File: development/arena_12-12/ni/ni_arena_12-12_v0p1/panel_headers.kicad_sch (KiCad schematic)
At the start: 27 parts, among them P1 CONN15, P10 CONN15, P11 CONN15, P12 CONN15, P2 CONN15, P3 CONN15, P4 CONN15, P5 CONN15, P6 CONN15, P7 CONN15, P8 CONN15, P9 CONN15, Q2 MOSFET_NCHAN

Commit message: Worked on schematic adding series termination resistors and buffers.
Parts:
- renumbered C11 to C1, C20 to C10, C21 to C11, C22 to C12, C12 to C2, C13 to C3, C14 to C4, C15 to C5, C16 to C6, C17 to C7, C18 to C8, C19 to C9, Q2 to Q1, R1 to R500, R2 to R501

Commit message: Worked on 12-12 NI arena schematic.
Added schmitt trigger buffers and series termination resistors to
panels headers (not done).
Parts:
- added C35, C36, C37, C38, C39, C40, C41, C42, C43, C44, C45, C46, C47, C48, C49, C50, C51, C52, C53, C54, C55, C56, C57, C58, C59, C60, C61, C62, C63, C64, C65, C66, C67, C68, C69, C70, C71, C72, C73, C74, C75, C76, C77, C78, C79, C80, C81, C82: 0.1uF, symbol Device:C_Small
- added R175, R176, R177, R178, R179, R180, R181, R182, R183, R184, R185, R186, R187, R188, R189, R190, R191, R192, R193, R194, R195, R196, R197, R198, R199, R200, R201, R202, R203, R204, R205, R206, R207, R208, R209, R210, R211, R212, R213, R214, R215, R216, R217, R218, R219, R220, R221, R222, R223, R224, R225, R226, R227, R228, R229, R230, R231, R232, R233, R234, R235, R236, R237, R238, R239, R240, R241, R242, R243, R244, R245, R246, R247, R248, R249, R250, R251, R252, R253, R254, R255, R256, R257, R258, R29, R30, R31, R32, R33, R34, R35, R36, R37, R38, R39, R40: 33, symbol Device:R
- added U39, U40, U41, U42, U43, U44, U45, U46, U47, U48, U49, U50, U51, U52, U53, U54, U55, U56, U57, U58, U59, U60, U61, U62, U63, U64, U65, U66, U67, U68, U69, U70, U71, U72, U73, U74, U75, U76, U77, U78, U79, U80, U81, U82, U83, U84, U85, U86: 74LVC2G17, symbol 74xGxx:74LVC2G17
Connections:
- net GND: now also C35.2, C36.2, C37.2, C38.2, C39.2, C40.2, C41.2, C42.2, C43.2, C44.2, C45.2, C46.2, C47.2, C48.2, C49.2, C50.2, C51.2, C52.2, C53.2, C54.2, C55.2, C56.2, C57.2, C58.2, C59.2, C60.2, C61.2, C62.2, C63.2, C64.2, C65.2, C66.2, C67.2, C68.2, C69.2, C70.2, C71.2, C72.2, C73.2, C74.2, C75.2, C76.2, C77.2, C78.2, C79.2, C80.2, C81.2, C82.2, U39.2 (GND), U40.2 (GND), U41.2 (GND), U42.2 (GND), U43.2 (GND), U44.2 (GND), U45.2 (GND), U46.2 (GND), U47.2 (GND), U48.2 (GND), U49.2 (GND), U50.2 (GND), U51.2 (GND), U52.2 (GND), U53.2 (GND), U54.2 (GND), U55.2 (GND), U56.2 (GND), U57.2 (GND), U58.2 (GND), U59.2 (GND), U60.2 (GND), U61.2 (GND), U62.2 (GND), U63.2 (GND), U64.2 (GND), U65.2 (GND), U66.2 (GND), U67.2 (GND), U68.2 (GND), U69.2 (GND), U70.2 (GND), U71.2 (GND), U72.2 (GND), U73.2 (GND), U74.2 (GND), U75.2 (GND), U76.2 (GND), U77.2 (GND), U78.2 (GND), U79.2 (GND), U80.2 (GND), U81.2 (GND), U82.2 (GND), U83.2 (GND), U84.2 (GND), U85.2 (GND), U86.2 (GND)
- net PAN5V.CS_00: no longer P1.7, P2.7, P3.7, P4.7, P5.7, P6.7, P7.7, P8.7
- net PAN5V.CS_01: no longer P1.8, P2.8, P3.8, P4.8, P5.8, P6.8, P7.8, P8.8
- net PAN5V.CS_02: no longer P1.9, P2.9, P3.9, P4.9, P5.9, P6.9, P7.9, P8.9
- net PAN5V.CS_03: no longer P1.10, P2.10, P3.10, P4.10, P5.10, P6.10, P7.10, P8.10
- net PAN5V.CS_04: no longer P1.11, P2.11, P3.11, P4.11, P5.11, P6.11, P7.11, P8.11
- net PAN5V.CS_05: no longer P1.12, P2.12, P3.12, P4.12, P5.12, P6.12, P7.12, P8.12
- net PAN5V.CS_06: no longer P1.13, P2.13, P3.13, P4.13, P5.13, P6.13, P7.13, P8.13
- net PAN5V.CS_07: no longer P1.14, P2.14, P3.14, P4.14, P5.14, P6.14, P7.14, P8.14
- net PAN5V.EXT_INT: now also U44.1, U50.1, U56.1, U62.1, U68.1, U74.1, U80.1, U86.1; no longer P1.15, P2.15, P3.15, P4.15, P5.15, P6.15, P7.15, P8.15
- net PAN5V.MISO_00: now also R31.1; no longer P1.6
- net PAN5V.MISO_01: now also R177.1; no longer P2.6
- net PAN5V.MISO_02: now also R189.1; no longer P3.6
- net PAN5V.MISO_03: now also R201.1; no longer P4.6
- net PAN5V.MISO_04: now also R213.1; no longer P5.6
- net PAN5V.MISO_05: now also R225.1; no longer P6.6
- net PAN5V.MISO_06: now also R237.1; no longer P7.6
- net PAN5V.MISO_07: now also R249.1; no longer P8.6
- net PAN5V.MOSI_00: now also U39.3; no longer P1.5
- net PAN5V.MOSI_01: now also U45.3; no longer P2.5
- net PAN5V.MOSI_02: now also U51.3; no longer P3.5
- net PAN5V.MOSI_03: now also U57.3; no longer P4.5
- net PAN5V.MOSI_04: now also U63.3; no longer P5.5
- net PAN5V.MOSI_05: now also U69.3; no longer P6.5
- net PAN5V.MOSI_06: now also U75.3; no longer P7.5
- net PAN5V.MOSI_07: now also U81.3; no longer P8.5
- net PAN5V.SCK_02: no longer P3.4
- net PAN5V.SCK_03: no longer P4.4
- net PAN5V.SCK_04: no longer P5.4
- net PAN5V.SCK_05: no longer P6.4
- net RESET: no longer P10.3, P11.3, P12.3, P9.3
- net PAN5V.SCK_00 renamed SCK_0_H1_P01
- net SCK_0_H1_P01: now also R29.2; no longer P7.4
- net PAN5V.SCK_01 renamed SCK_1_H1_P02
- net SCK_1_H1_P02: now also R175.2; no longer P8.4
- new net: R229.1, U71.4
- new net: R194.1, U54.6
- new net: R247.1, U81.6
- new net: R245.1, U79.4
- new net: R238.1, U76.6
- new net: R256.1, U85.6
- new net: R196.1, U55.6
- new net: R208.1, U61.6
- new net: R176.1, U45.4
- new net: R206.1, U60.6
- new net: R184.1, U49.6
- new net: R193.1, U53.4
- new net: R257.1, U85.4
- new net: R35.1, U41.4
- new net: R199.1, U57.6
- new net: R30.1, U39.4
- new net: R217.1, U65.4
- new net: R187.1, U51.6
- new net: R212.1, U63.4
- new net: R255.1, U84.4
- new net: R210.1, U62.6
- new net: R205.1, U59.4
- new net: R250.1, U82.6
- new net: R211.1, U63.6
- new net: R178.1, U46.6
- new net: R246.1, U80.6
- new net: R226.1, U70.6
- new net: R188.1, U51.4
- new net: R248.1, U81.4
- new net: R215.1, U64.4
- new net: R231.1, U72.4
- new net: R243.1, U78.4
- new net: R239.1, U76.4
- new net: R233.1, U73.4
- new net: R181.1, U47.4
- new net: R236.1, U75.4
- new net: R195.1, U54.4
- new net: R230.1, U72.6
- new net: R185.1, U49.4
- new net: R183.1, U48.4
- new net: R244.1, U79.6
- new net: R227.1, U70.4
- new net: R197.1, U55.4
- new net: R214.1, U64.6
- new net: R38.1, U43.6
- new net: R39.1, U43.4
- new net: R203.1, U58.4
- new net: R254.1, U84.6
- new net: R190.1, U52.6
- new net: R218.1, U66.6
- new net: R175.1, U45.6
- new net: R216.1, U65.6
- new net: R180.1, U47.6
- new net: R224.1, U69.4
- new net: R223.1, U69.6
- new net: R251.1, U82.4
- new net: R204.1, U59.6
- new net: R192.1, U53.6
- new net: R228.1, U71.6
- new net: R202.1, U58.6
- new net: R191.1, U52.4
- new net: R36.1, U42.6
- new net: R209.1, U61.4
- new net: R258.1, U86.6
- new net: R179.1, U46.4
- new net: R207.1, U60.4
- new net: R200.1, U57.4
- new net: R234.1, U74.6
- new net: R220.1, U67.6
- new net: R198.1, U56.6
- new net: R221.1, U67.4
- new net: R182.1, U48.6
- new net: R33.1, U40.4
- new net: R242.1, U78.6
- new net: R29.1, U39.6
- new net: R252.1, U83.6
- new net: R240.1, U77.6
- new net: R241.1, U77.4
- new net: R37.1, U42.4
- new net: R219.1, U66.4
- new net: R34.1, U41.6
- new net: R235.1, U75.6
- new net: R40.1, U44.6
- new net: R232.1, U73.6
- new net: R253.1, U83.4
- new net: R32.1, U40.6
- new net: R186.1, U50.6
- new net: R222.1, U68.6
- new net +3.3V: C35.1, C36.1, C37.1, C38.1, C39.1, C40.1, C41.1, C42.1, C43.1, C44.1, C45.1, C46.1, C47.1, C48.1, C49.1, C50.1, C51.1, C52.1, C53.1, C54.1, C55.1, C56.1, C57.1, C58.1, C59.1, C60.1, C61.1, C62.1, C63.1, C64.1, C65.1, C66.1, C67.1, C68.1, C69.1, C70.1, C71.1, C72.1, C73.1, C74.1, C75.1, C76.1, C77.1, C78.1, C79.1, C80.1, C81.1, C82.1, U39.5 (VCC), U40.5 (VCC), U41.5 (VCC), U42.5 (VCC), U43.5 (VCC), U44.5 (VCC), U45.5 (VCC), U46.5 (VCC), U47.5 (VCC), U48.5 (VCC), U49.5 (VCC), U50.5 (VCC), U51.5 (VCC), U52.5 (VCC), U53.5 (VCC), U54.5 (VCC), U55.5 (VCC), U56.5 (VCC), U57.5 (VCC), U58.5 (VCC), U59.5 (VCC), U60.5 (VCC), U61.5 (VCC), U62.5 (VCC), U63.5 (VCC), U64.5 (VCC), U65.5 (VCC), U66.5 (VCC), U67.5 (VCC), U68.5 (VCC), U69.5 (VCC), U70.5 (VCC), U71.5 (VCC), U72.5 (VCC), U73.5 (VCC), U74.5 (VCC), U75.5 (VCC), U76.5 (VCC), U77.5 (VCC), U78.5 (VCC), U79.5 (VCC), U80.5 (VCC), U81.5 (VCC), U82.5 (VCC), U83.5 (VCC), U84.5 (VCC), U85.5 (VCC), U86.5 (VCC)
- new net CS_00_P01: P1.7, R32.2
- new net CS_00_P02: P2.7, R178.2
- new net CS_00_P03: P3.7, R190.2
- new net CS_00_P04: P4.7, R202.2
- new net CS_00_P05: P5.7, R214.2
- new net CS_00_P06: P6.7, R226.2
- new net CS_00_P07: P7.7, R238.2
- new net CS_00_P08: P8.7, R250.2
- new net CS_01_P01: P1.8, R33.2
- new net CS_01_P02: P2.8, R179.2
- new net CS_01_P03: P3.8, R191.2
- new net CS_01_P04: P4.8, R203.2
- new net CS_01_P05: P5.8, R215.2
- new net CS_01_P06: P6.8, R227.2
- new net CS_01_P07: P7.8, R239.2
- new net CS_01_P08: P8.8, R251.2
- new net CS_02_P01: P1.9, R34.2
- new net CS_02_P02: P2.9, R180.2
- new net CS_02_P03: P3.9, R192.2
- new net CS_02_P04: P4.9, R204.2
- new net CS_02_P05: P5.9, R216.2
- new net CS_02_P06: P6.9, R228.2
- new net CS_02_P07: P7.9, R240.2
- new net CS_02_P08: P8.9, R252.2
- new net CS_03_P01: P1.10, R35.2
- new net CS_03_P02: P2.10, R181.2
- new net CS_03_P03: P3.10, R193.2
- new net CS_03_P04: P4.10, R205.2
- new net CS_03_P05: P5.10, R217.2
- new net CS_03_P06: P6.10, R229.2
- new net CS_03_P07: P7.10, R241.2
- new net CS_03_P08: P8.10, R253.2
- new net CS_04_P01: P1.11, R36.2
- new net CS_04_P02: P2.11, R182.2
- new net CS_04_P03: P3.11, R194.2
- new net CS_04_P04: P4.11, R206.2
- new net CS_04_P05: P5.11, R218.2
- new net CS_04_P06: P6.11, R230.2
- new net CS_04_P07: P7.11, R242.2
- new net CS_04_P08: P8.11, R254.2
- new net CS_05_P01: P1.12, R37.2
- new net CS_05_P02: P2.12, R183.2
- new net CS_05_P03: P3.12, R195.2
- new net CS_05_P04: P4.12, R207.2
- new net CS_05_P05: P5.12, R219.2
- new net CS_05_P06: P6.12, R231.2
- new net CS_05_P07: P7.12, R243.2
- new net CS_05_P08: P8.12, R255.2
- new net CS_06_P01: P1.13, R38.2
- new net CS_06_P02: P2.13, R184.2
- new net CS_06_P03: P3.13, R196.2
- new net CS_06_P04: P4.13, R208.2
- new net CS_06_P05: P5.13, R220.2
- new net CS_06_P06: P6.13, R232.2
- new net CS_06_P07: P7.13, R244.2
- new net CS_06_P08: P8.13, R256.2
- new net CS_07_P01: P1.14, R39.2
- new net CS_07_P02: P2.14, R185.2
- new net CS_07_P03: P3.14, R197.2
- new net CS_07_P04: P4.14, R209.2
- new net CS_07_P05: P5.14, R221.2
- new net CS_07_P06: P6.14, R233.2
- new net CS_07_P07: P7.14, R245.2
- new net CS_07_P08: P8.14, R257.2
- new net EXT_INT_P01: P1.15, R40.2
- new net EXT_INT_P02: P2.15, R186.2
- new net EXT_INT_P03: P3.15, R198.2
- new net EXT_INT_P04: P4.15, R210.2
- new net EXT_INT_P05: P5.15, R222.2
- new net EXT_INT_P06: P6.15, R234.2
- new net EXT_INT_P07: P7.15, R246.2
- new net EXT_INT_P08: P8.15, R258.2
- new net MISO_00_P01: P1.6, R31.2
- new net MISO_01_P02: P2.6, R177.2
- new net MISO_02_P03: P3.6, R189.2
- new net MISO_03_P04: P4.6, R201.2
- new net MISO_04_P05: P5.6, R213.2
- new net MISO_05_P06: P6.6, R225.2
- new net MISO_06_P07: P7.6, R237.2
- new net MISO_07_P08: P8.6, R249.2
- new net MOSI_00_P01: P1.5, R30.2
- new net MOSI_01_P02: P2.5, R176.2
- new net MOSI_02_P03: P3.5, R188.2
- new net MOSI_03_P04: P4.5, R200.2
- new net MOSI_04_P05: P5.5, R212.2
- new net MOSI_05_P06: P6.5, R224.2
- new net MOSI_06_P07: P7.5, R236.2
- new net MOSI_07_P08: P8.5, R248.2
- new net PAN5V.CS_0_P01: U40.1
- new net PAN5V.CS_0_P02: U46.1
- new net PAN5V.CS_0_P03: U52.1
- new net PAN5V.CS_0_P04: U58.1
- new net PAN5V.CS_0_P05: U64.1
- new net PAN5V.CS_0_P06: U70.1
- new net PAN5V.CS_0_P07: U76.1
- new net PAN5V.CS_0_P08: U82.1
- new net PAN5V.CS_1_P01: U40.3
- new net PAN5V.CS_1_P02: U46.3
- new net PAN5V.CS_1_P03: U52.3
- new net PAN5V.CS_1_P04: U58.3
- new net PAN5V.CS_1_P05: U64.3
- new net PAN5V.CS_1_P06: U70.3
- new net PAN5V.CS_1_P07: U76.3
- new net PAN5V.CS_1_P08: U82.3
- new net PAN5V.CS_2_P01: U41.1
- new net PAN5V.CS_2_P02: U47.1
- new net PAN5V.CS_2_P03: U53.1
- new net PAN5V.CS_2_P04: U59.1
- new net PAN5V.CS_2_P05: U65.1
- new net PAN5V.CS_2_P06: U71.1
- new net PAN5V.CS_2_P07: U77.1
- new net PAN5V.CS_2_P08: U83.1
- new net PAN5V.CS_3_P01: U41.3
- new net PAN5V.CS_3_P02: U47.3
- new net PAN5V.CS_3_P03: U53.3
- new net PAN5V.CS_3_P04: U59.3
- new net PAN5V.CS_3_P05: U65.3
- new net PAN5V.CS_3_P06: U71.3
- new net PAN5V.CS_3_P07: U77.3
- new net PAN5V.CS_3_P08: U83.3
- new net PAN5V.CS_4_P01: U42.1
- new net PAN5V.CS_4_P02: U48.1
- new net PAN5V.CS_4_P03: U54.1
- new net PAN5V.CS_4_P04: U60.1
- new net PAN5V.CS_4_P05: U66.1
- new net PAN5V.CS_4_P06: U72.1
- new net PAN5V.CS_4_P07: U78.1
- new net PAN5V.CS_4_P08: U84.1
- new net PAN5V.CS_5_P01: U42.3
- new net PAN5V.CS_5_P02: U48.3
- new net PAN5V.CS_5_P03: U54.3
- new net PAN5V.CS_5_P04: U60.3
- new net PAN5V.CS_5_P05: U66.3
- new net PAN5V.CS_5_P06: U72.3
- new net PAN5V.CS_5_P07: U78.3
- new net PAN5V.CS_5_P08: U84.3
- new net PAN5V.CS_6_P01: U43.1
- new net PAN5V.CS_6_P02: U49.1
- new net PAN5V.CS_6_P03: U55.1
- new net PAN5V.CS_6_P04: U61.1
- new net PAN5V.CS_6_P05: U67.1
- new net PAN5V.CS_6_P06: U73.1
- new net PAN5V.CS_6_P07: U79.1
- new net PAN5V.CS_6_P08: U85.1
- new net PAN5V.CS_7_P01: U43.3
- new net PAN5V.CS_7_P02: U49.3
- new net PAN5V.CS_7_P03: U55.3
- new net PAN5V.CS_7_P04: U61.3
- new net PAN5V.CS_7_P05: U67.3
- new net PAN5V.CS_7_P06: U73.3
- new net PAN5V.CS_7_P07: U79.3
- new net PAN5V.CS_7_P08: U85.3
- new net PAN5V.SCK_0_H1: U39.1
- new net PAN5V.SCK_0_H2: U75.1
- new net PAN5V.SCK_1_H1: U45.1
- new net PAN5V.SCK_1_H2: U81.1
- new net PAN5V.SCK_2_H1: U51.1
- new net PAN5V.SCK_3_H1: U57.1
- new net PAN5V.SCK_4_H1: U63.1
- new net PAN5V.SCK_5_H1: U69.1
- new net SCK_0_H2_P07: P7.4, R235.2
- new net SCK_1_H2_P08: P8.4, R247.2
- new net SCK_2_H1_P03: P3.4, R187.2
- new net SCK_3_H1_P04: P4.4, R199.2
- new net SCK_4_H1_P05: P5.4, R211.2
- new net SCK_5_H1_P06: P6.4, R223.2
- no-connect marks 0 -> 16
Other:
- note added: "SI2302-TP Digikey SI2302-TPMSCT-ND LCSC C4748714 or ME2306D LCSC C165220"
- note removed: "SI2302-TP Digikey SI2302-TPMSCT-ND LCSC C4748714"
- moved on the sheet: C1, C10, C11, C12, C9, P1, P10, P11, P12, P9, Q1, R500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

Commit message: More work on 12-12 NI arena panels headers sheet.
Changes schmitt trigger power to 5V instead 3.3V.  Finished Panels
column P9.
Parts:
- added C84, C85, C86, C87, C88, C89: 0.1uF, symbol Device:C_Small
- added R259, R260, R261, R262, R263, R264, R265, R266, R267, R268, R269, R270: 33, symbol Device:R
- added U87, U88, U89, U90, U91, U92: 74LVC2G17, symbol 74xGxx:74LVC2G17
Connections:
- net +3.3V is gone; now on net +5V: C35.1, C36.1, C37.1, C38.1, C39.1, C40.1, C41.1, C42.1, C43.1, C44.1, C45.1, C46.1, C47.1, C48.1, C49.1, C50.1, C51.1, C52.1, C53.1, C54.1, C55.1, C56.1, C57.1, C58.1, C59.1, C60.1, C61.1, C62.1, C63.1, C64.1, C65.1, C66.1, C67.1, C68.1, C69.1, C70.1, C71.1, C72.1, C73.1, C74.1, C75.1, C76.1, C77.1, C78.1, C79.1, C80.1, C81.1, C82.1, U39.5 (VCC), U40.5 (VCC), U41.5 (VCC), U42.5 (VCC), U43.5 (VCC), U44.5 (VCC), U45.5 (VCC), U46.5 (VCC), U47.5 (VCC), U48.5 (VCC), U49.5 (VCC), U50.5 (VCC), U51.5 (VCC), U52.5 (VCC), U53.5 (VCC), U54.5 (VCC), U55.5 (VCC), U56.5 (VCC), U57.5 (VCC), U58.5 (VCC), U59.5 (VCC), U60.5 (VCC), U61.5 (VCC), U62.5 (VCC), U63.5 (VCC), U64.5 (VCC), U65.5 (VCC), U66.5 (VCC), U67.5 (VCC), U68.5 (VCC), U69.5 (VCC), U70.5 (VCC), U71.5 (VCC), U72.5 (VCC), U73.5 (VCC), U74.5 (VCC), U75.5 (VCC), U76.5 (VCC), U77.5 (VCC), U78.5 (VCC), U79.5 (VCC), U80.5 (VCC), U81.5 (VCC), U82.5 (VCC), U83.5 (VCC), U84.5 (VCC), U85.5 (VCC), U86.5 (VCC)
- net +5V: now also C84.1, C85.1, C86.1, C87.1, C88.1, C89.1, U87.5 (VCC), U88.5 (VCC), U89.5 (VCC), U90.5 (VCC), U91.5 (VCC), U92.5 (VCC)
- net GND: now also C84.2, C85.2, C86.2, C87.2, C88.2, C89.2, U87.2 (GND), U88.2 (GND), U89.2 (GND), U90.2 (GND), U91.2 (GND), U92.2 (GND)
- net PAN5V.CS_00: no longer P9.7
- net PAN5V.CS_01: no longer P9.8
- net PAN5V.CS_02: no longer P9.9
- net PAN5V.CS_03: no longer P9.10
- net PAN5V.CS_04: no longer P9.11
- net PAN5V.CS_05: no longer P9.12
- net PAN5V.CS_06: no longer P9.13
- net PAN5V.CS_07: no longer P9.14
- net PAN5V.CS_0_P09: now also U88.1
- net PAN5V.CS_1_P09: now also U88.3
- net PAN5V.CS_2_P09: now also U89.1
- net PAN5V.CS_3_P09: now also U89.3
- net PAN5V.CS_4_P09: now also U90.1
- net PAN5V.CS_5_P09: now also U90.3
- net PAN5V.CS_6_P09: now also U91.1
- net PAN5V.CS_7_P09: now also U91.3
- net PAN5V.EXT_INT: now also U92.1; no longer P9.15
- net PAN5V.MISO_08: now also R261.1; no longer P9.6
- net PAN5V.MOSI_08: now also U87.3; no longer P9.5
- net PAN5V.SCK_2_H2: now also U87.1
- net RESET: now also P9.3
- net PAN5V.SCK_02 renamed SCK_2_H2_P09
- net SCK_2_H2_P09: now also R259.2
- new net: R268.1, U91.6
- new net: R265.1, U89.4
- new net: R266.1, U90.6
- new net: R264.1, U89.6
- new net: R263.1, U88.4
- new net: R269.1, U91.4
- new net: R262.1, U88.6
- new net: R270.1, U92.6
- new net: R260.1, U87.4
- new net: R267.1, U90.4
- new net: R259.1, U87.6
- new net CS_00_P09: P9.7, R262.2
- new net CS_01_P09: P9.8, R263.2
- new net CS_02_P09: P9.9, R264.2
- new net CS_03_P09: P9.10, R265.2
- new net CS_04_P09: P9.11, R266.2
- new net CS_05_P09: P9.12, R267.2
- new net CS_06_P09: P9.13, R268.2
- new net CS_07_P09: P9.14, R269.2
- new net EXT_INT_P09: P9.15, R270.2
- new net MISO_08_P09: P9.6, R261.2
- new net MOSI_08_P09: P9.5, R260.2
- no-connect marks 16 -> 18

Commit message: Finished initial schematic for 12-12 NI with schmitt buffers.
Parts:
- added C100, C101, C102, C103, C104, C105, C106, C107, C90, C91, C92, C93, C94, C95, C96, C97, C98, C99: 0.1uF, symbol Device:C_Small
- added R271, R272, R273, R274, R275, R276, R277, R278, R279, R280, R281, R282, R283, R284, R285, R286, R287, R288, R289, R290, R291, R292, R293, R294, R295, R296, R297, R298, R299, R300, R301, R302, R303, R304, R305, R306: 33, symbol Device:R
- added U100, U101, U102, U103, U104, U105, U106, U107, U108, U109, U110, U93, U94, U95, U96, U97, U98, U99: 74LVC2G17, symbol 74xGxx:74LVC2G17
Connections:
- net +5V: now also C100.1, C101.1, C102.1, C103.1, C104.1, C105.1, C106.1, C107.1, C90.1, C91.1, C92.1, C93.1, C94.1, C95.1, C96.1, C97.1, C98.1, C99.1, U100.5 (VCC), U101.5 (VCC), U102.5 (VCC), U103.5 (VCC), U104.5 (VCC), U105.5 (VCC), U106.5 (VCC), U107.5 (VCC), U108.5 (VCC), U109.5 (VCC), U110.5 (VCC), U93.5 (VCC), U94.5 (VCC), U95.5 (VCC), U96.5 (VCC), U97.5 (VCC), U98.5 (VCC), U99.5 (VCC)
- net GND: now also C100.2, C101.2, C102.2, C103.2, C104.2, C105.2, C106.2, C107.2, C90.2, C91.2, C92.2, C93.2, C94.2, C95.2, C96.2, C97.2, C98.2, C99.2, U100.2 (GND), U101.2 (GND), U102.2 (GND), U103.2 (GND), U104.2 (GND), U105.2 (GND), U106.2 (GND), U107.2 (GND), U108.2 (GND), U109.2 (GND), U110.2 (GND), U93.2 (GND), U94.2 (GND), U95.2 (GND), U96.2 (GND), U97.2 (GND), U98.2 (GND), U99.2 (GND)
- net PAN5V.CS_0_P10: now also U94.1
- net PAN5V.CS_0_P11: now also U100.1
- net PAN5V.CS_0_P12: now also U106.1
- net PAN5V.CS_1_P10: now also U94.3
- net PAN5V.CS_1_P11: now also U100.3
- net PAN5V.CS_1_P12: now also U106.3
- net PAN5V.CS_2_P10: now also U95.1
- net PAN5V.CS_2_P11: now also U101.1
- net PAN5V.CS_2_P12: now also U107.1
- net PAN5V.CS_3_P10: now also U95.3
- net PAN5V.CS_3_P11: now also U101.3
- net PAN5V.CS_3_P12: now also U107.3
- net PAN5V.CS_4_P10: now also U96.1
- net PAN5V.CS_4_P11: now also U102.1
- net PAN5V.CS_4_P12: now also U108.1
- net PAN5V.CS_5_P10: now also U96.3
- net PAN5V.CS_5_P11: now also U102.3
- net PAN5V.CS_5_P12: now also U108.3
- net PAN5V.CS_6_P10: now also U97.1
- net PAN5V.CS_6_P11: now also U103.1
- net PAN5V.CS_6_P12: now also U109.1
- net PAN5V.CS_7_P10: now also U97.3
- net PAN5V.CS_7_P11: now also U103.3
- net PAN5V.CS_7_P12: now also U109.3
- net PAN5V.EXT_INT: now also U104.1, U110.1, U98.1; no longer P10.15, P11.15, P12.15
- net PAN5V.MISO_09: now also R273.1; no longer P10.6
- net PAN5V.MISO_10: now also R285.1; no longer P11.6
- net PAN5V.MISO_11: now also R297.1; no longer P12.6
- net PAN5V.MOSI_09: now also U93.3; no longer P10.5
- net PAN5V.MOSI_10: now also U99.3; no longer P11.5
- net PAN5V.MOSI_11: now also U105.3; no longer P12.5
- net PAN5V.SCK_3_H2: now also U93.1
- net PAN5V.SCK_4_H2: now also U99.1
- net PAN5V.SCK_5_H2: now also U105.1
- net RESET: now also P10.3, P11.3, P12.3
- removed net PAN5V.CS_00: P10.7, P11.7, P12.7
- removed net PAN5V.CS_01: P10.8, P11.8, P12.8
- removed net PAN5V.CS_02: P10.9, P11.9, P12.9
- removed net PAN5V.CS_03: P10.10, P11.10, P12.10
- removed net PAN5V.CS_04: P10.11, P11.11, P12.11
- removed net PAN5V.CS_05: P10.12, P11.12, P12.12
- removed net PAN5V.CS_06: P10.13, P11.13, P12.13
- removed net PAN5V.CS_07: P10.14, P11.14, P12.14
- net PAN5V.SCK_03 renamed SCK_3_H2_P10
- net SCK_3_H2_P10: now also R271.2
- net PAN5V.SCK_04 renamed SCK_4_H2_P11
- net SCK_4_H2_P11: now also R283.2
- net PAN5V.SCK_05 renamed SCK_5_H2_P12
- net SCK_5_H2_P12: now also R295.2
- new net: R287.1, U100.4
- new net: R304.1, U109.6
- new net: R279.1, U96.4
- new net: R294.1, U104.6
- new net: R281.1, U97.4
- new net: R301.1, U107.4
- new net: R272.1, U93.4
- new net: R293.1, U103.4
- new net: R306.1, U110.6
- new net: R280.1, U97.6
- new net: R303.1, U108.4
- new net: R300.1, U107.6
- new net: R289.1, U101.4
- new net: R277.1, U95.4
- new net: R286.1, U100.6
- new net: R283.1, U99.6
- new net: R278.1, U96.6
- new net: R298.1, U106.6
- new net: R276.1, U95.6
- new net: R291.1, U102.4
- new net: R282.1, U98.6
- new net: R271.1, U93.6
- new net: R288.1, U101.6
- new net: R302.1, U108.6
- new net: R295.1, U105.6
- new net: R292.1, U103.6
- new net: R290.1, U102.6
- new net: R284.1, U99.4
- new net: R275.1, U94.4
- new net: R299.1, U106.4
- new net: R296.1, U105.4
- new net: R305.1, U109.4
- new net: R274.1, U94.6
- new net CS_00_P10: P10.7, R274.2
- new net CS_00_P11: P11.7, R286.2
- new net CS_00_P12: P12.7, R298.2
- new net CS_01_P10: P10.8, R275.2
- new net CS_01_P11: P11.8, R287.2
- new net CS_01_P12: P12.8, R299.2
- new net CS_02_P10: P10.9, R276.2
- new net CS_02_P11: P11.9, R288.2
- new net CS_02_P12: P12.9, R300.2
- new net CS_03_P10: P10.10, R277.2
- new net CS_03_P11: P11.10, R289.2
- new net CS_03_P12: P12.10, R301.2
- new net CS_04_P10: P10.11, R278.2
- new net CS_04_P11: P11.11, R290.2
- new net CS_04_P12: P12.11, R302.2
- new net CS_05_P10: P10.12, R279.2
- new net CS_05_P11: P11.12, R291.2
- new net CS_05_P12: P12.12, R303.2
- new net CS_06_P10: P10.13, R280.2
- new net CS_06_P11: P11.13, R292.2
- new net CS_06_P12: P12.13, R304.2
- new net CS_07_P10: P10.14, R281.2
- new net CS_07_P11: P11.14, R293.2
- new net CS_07_P12: P12.14, R305.2
- new net EXT_INT_P10: P10.15, R282.2
- new net EXT_INT_P11: P11.15, R294.2
- new net EXT_INT_P12: P12.15, R306.2
- new net MISO_09_P10: P10.6, R273.2
- new net MISO_10_P11: P11.6, R285.2
- new net MISO_11_P12: P12.6, R297.2
- new net MOSI_09_P10: P10.5, R272.2
- new net MOSI_10_P11: P11.5, R284.2
- new net MOSI_11_P12: P12.5, R296.2
- no-connect marks 18 -> 24
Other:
- moved on the sheet: C1, C2, C3, C35, C36, C37, C38, C39, C4, C40, C41, C42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

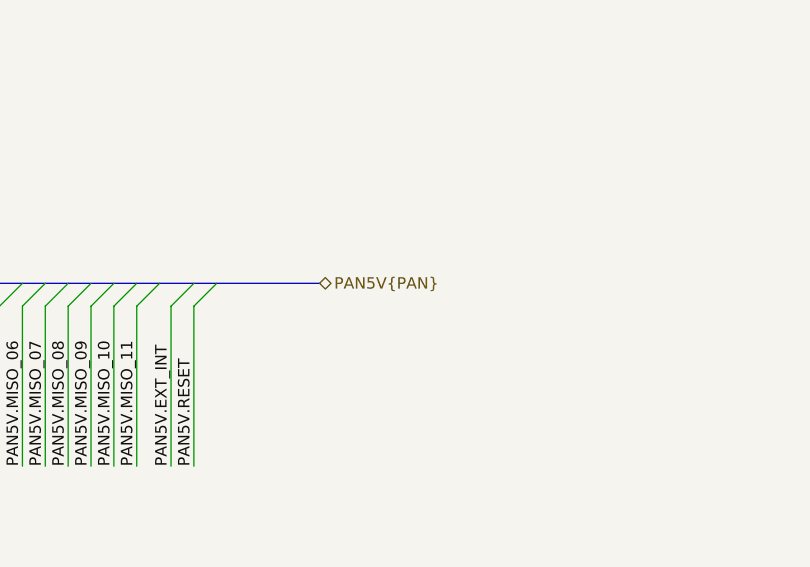
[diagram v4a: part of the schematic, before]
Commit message: Worked on NI 12-12 arena schematic.
Set up new bus definitions and started working through DRC issues.
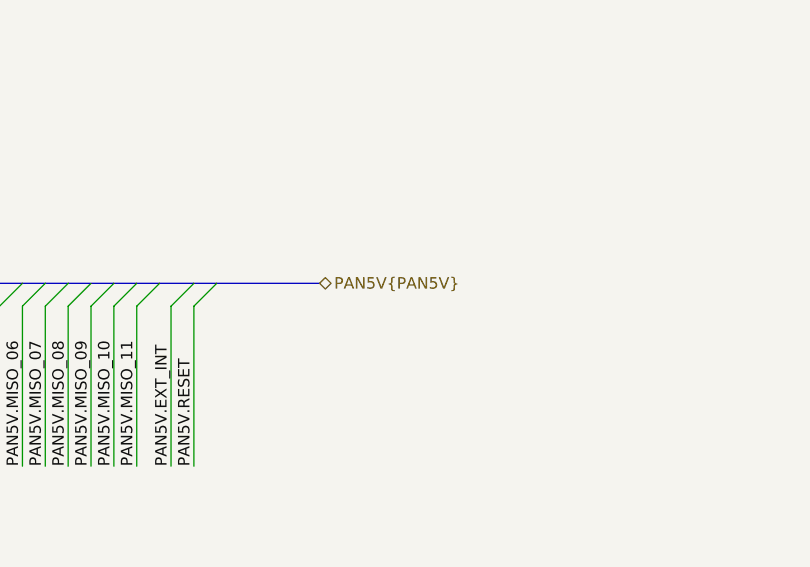
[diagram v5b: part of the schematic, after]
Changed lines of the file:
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@@
 		)
 	)
-	(hierarchical_label "PAN5V{PAN}"
+	(hierarchical_label "PAN5V{PAN5V}"
 		(shape bidirectional)
 		(at 574.04 739.14 0)

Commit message: Worked on 12-12 NI arena with schmitt buffers.
Finished footprint assignments.
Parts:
- C100: renamed from C101; footprint (none) -> Capacitor_SMD:C_0402_1005Metric
- C101: renamed from C102; footprint (none) -> Capacitor_SMD:C_0402_1005Metric
- C102: renamed from C103; footprint (none) -> Capacitor_SMD:C_0402_1005Metric
- C103: renamed from C104; footprint (none) -> Capacitor_SMD:C_0402_1005Metric
- C104: renamed from C105; footprint (none) -> Capacitor_SMD:C_0402_1005Metric
- C105: renamed from C106; footprint (none) -> Capacitor_SMD:C_0402_1005Metric
- C106: renamed from C107; footprint (none) -> Capacitor_SMD:C_0402_1005Metric
- C35, C36, C37, C38, C39, C40, C41, C42, C43, C44, C45, C46, C47, C48, C49, C50, C51, C52, C53, C54, C55, C56, C57, C58, C59, C60, C61, C62, C63, C64, C65, C66, C67, C68, C69, C70, C71, C72, C73, C74, C75, C76, C77, C78, C79, C80, C81, C82: footprint (none) -> Capacitor_SMD:C_0402_1005Metric
- C83: renamed from C84; footprint (none) -> Capacitor_SMD:C_0402_1005Metric
- C84: renamed from C85; footprint (none) -> Capacitor_SMD:C_0402_1005Metric
- C85: renamed from C86; footprint (none) -> Capacitor_SMD:C_0402_1005Metric
- C86: renamed from C87; footprint (none) -> Capacitor_SMD:C_0402_1005Metric
- C87: renamed from C88; footprint (none) -> Capacitor_SMD:C_0402_1005Metric
- C88: renamed from C89; footprint (none) -> Capacitor_SMD:C_0402_1005Metric
- C89: renamed from C90; footprint (none) -> Capacitor_SMD:C_0402_1005Metric
- C90: renamed from C91; footprint (none) -> Capacitor_SMD:C_0402_1005Metric
- C91: renamed from C92; footprint (none) -> Capacitor_SMD:C_0402_1005Metric
- C92: renamed from C93; footprint (none) -> Capacitor_SMD:C_0402_1005Metric
- C93: renamed from C94; footprint (none) -> Capacitor_SMD:C_0402_1005Metric
- C94: renamed from C95; footprint (none) -> Capacitor_SMD:C_0402_1005Metric
- C95: renamed from C96; footprint (none) -> Capacitor_SMD:C_0402_1005Metric
- C96: renamed from C97; footprint (none) -> Capacitor_SMD:C_0402_1005Metric
- C97: renamed from C98; footprint (none) -> Capacitor_SMD:C_0402_1005Metric
- C98: renamed from C99; footprint (none) -> Capacitor_SMD:C_0402_1005Metric
- C99: renamed from C100; footprint (none) -> Capacitor_SMD:C_0402_1005Metric
- R175, R176, R177, R178, R179, R180, R181, R182, R183, R184, R185, R186, R187, R188, R189, R190, R191, R192, R193, R194, R195, R196, R197, R198, R199, R200, R201, R202, R203, R204, R205, R206, R207, R208, R209, R210, R211, R212, R213, R214, R215, R216, R217, R218, R219, R220, R221, R222, R223, R224, R225, R226, R227, R228, R229, R230, R231, R232, R233, R234, R235, R236, R237, R238, R239, R240, R241, R242, R243, R244, R245, R246, R247, R248, R249, R250, R251, R252, R253, R254, R255, R256, R257, R258, R259, R260, R261, R262, R263, R264, R265, R266, R267, R268, R269, R270, R271, R272, R273, R274, R275, R276, R277, R278, R279, R280, R281, R282, R283, R284, R285, R286, R287, R288, R289, R29, R290, R291, R292, R293, R294, R295, R296, R297, R298, R299, R30, R300, R301, R302, R303, R304, R305, R306, R31, R32, R33, R34, R35, R36, R37, R38, R39, R40: footprint (none) -> Resistor_SMD:R_0402_1005Metric
- R307: renamed from R501; footprint Resistor_SMD:R_0805_2012Metric -> Resistor_SMD:R_0402_1005Metric
- R308: renamed from R500; footprint Resistor_SMD:R_0805_2012Metric -> Resistor_SMD:R_0402_1005Metric
- U100, U101, U102, U103, U104, U105, U106, U107, U108, U109, U110, U39, U40, U41, U42, U43, U44, U45, U46, U47, U48, U49, U50, U51, U52, U53, U54, U55, U56, U57, U58, U59, U60, U61, U62, U63, U64, U65, U66, U67, U68, U69, U70, U71, U72, U73, U74, U75, U76, U77, U78, U79, U80, U81, U82, U83, U84, U85, U86, U87, U88, U89, U90, U91, U92, U93, U94, U95, U96, U97, U98, U99: footprint (none) -> Package_TO_SOT_SMD:SOT-23-6
